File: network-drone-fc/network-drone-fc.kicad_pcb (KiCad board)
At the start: 4 copper layers, 27 x 27 mm, 4 parts

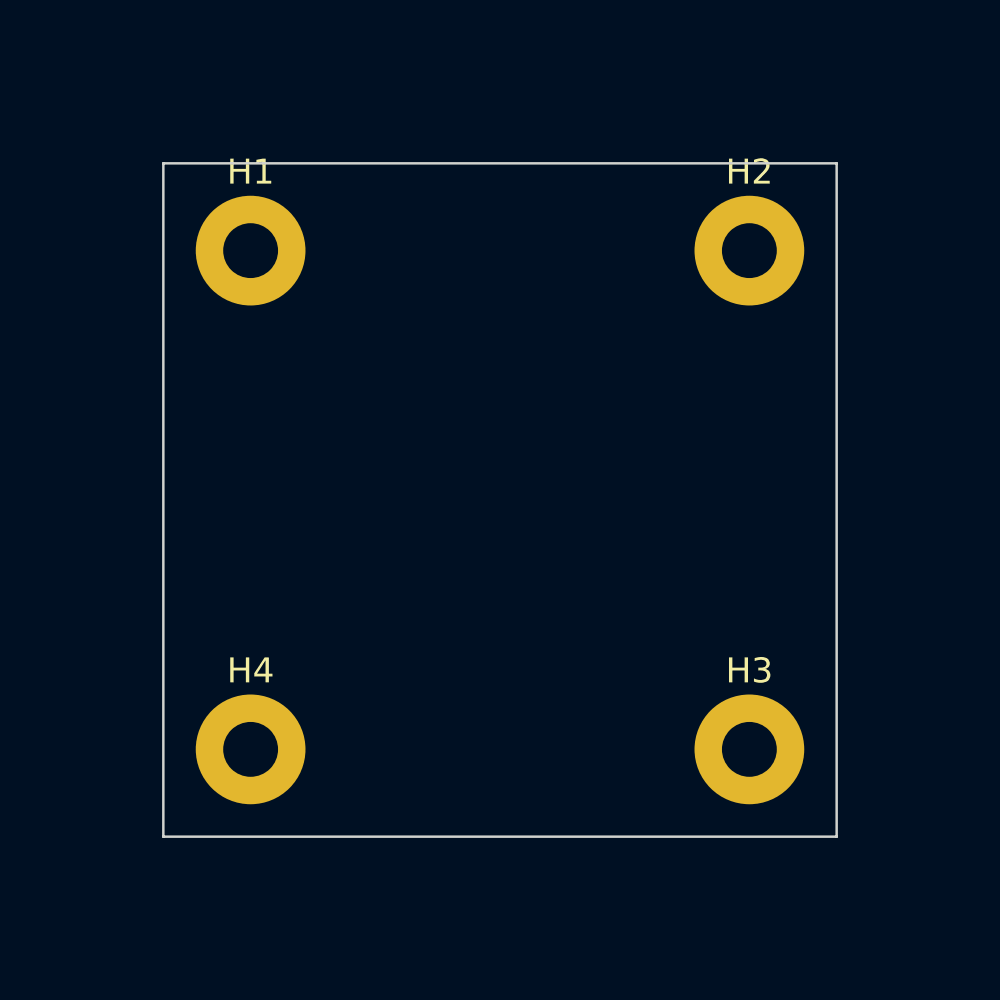
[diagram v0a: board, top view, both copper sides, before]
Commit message: Grow board to 36x36 mm so all parts fit on one side for hot-plate reflow
Keeps the 20x20 M2 holes to stack on the smaller ESC.
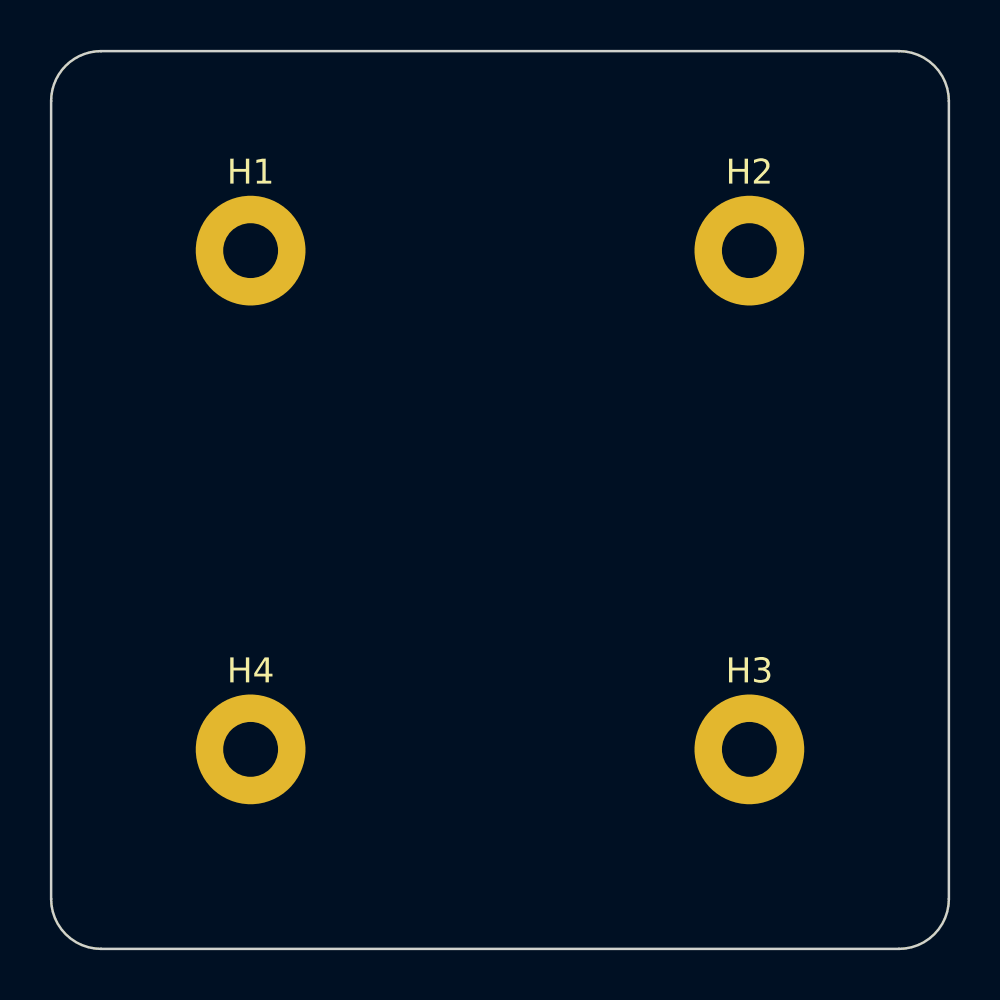
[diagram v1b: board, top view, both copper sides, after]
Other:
- board size 27 x 27 mm -> 36 x 36 mm
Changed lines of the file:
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@@
 		(embedded_fonts no)
 	)
-	(gr_line
-		(start 86.5 86.5)
-		(end 113.5 86.5)
+	(gr_arc
+		(start 116 82)
+		(mid 117.414213 82.585786)
+		(end 118 84)
 		(stroke
 			(width 0.1)
@@
 	)
 	(gr_line
-		(start 113.5 113.5)
-		(end 86.5 113.5)
+		(start 118 84)
+		(end 118 116)
+		(stroke
+			(width 0.1)
+			(type default)
+		)
+		(layer "Edge.Cuts")
+	)
+	(gr_arc
+		(start 82 84)
+		(mid 82.585786 82.585786)
+		(end 84 82)
 		(stroke
 			(width 0.1)
@@
 	)
 	(gr_line
-		(start 113.5 86.5)
-		(end 113.5 113.5)
+		(start 116 118)
+		(end 84 118)
+		(stroke
+			(width 0.1)
+			(type default)
+		)
+		(layer "Edge.Cuts")
+	)
+	(gr_arc
+		(start 84 118)
+		(mid 82.585786 117.414213)
+		(end 82 116)
 		(stroke
 			(width 0.1)
@@
 	)
 	(gr_line
-		(start 86.5 113.5)
-		(end 86.5 86.5)
+		(start 84 82)
+		(end 116 82)
 		(stroke
 			(width 0.1)
+			(type default)
+		)
+		(layer "Edge.Cuts")
+	)
+	(gr_line
+		(start 82 116)
+		(end 82 84)
+		(stroke
+			(width 0.1)
+			(type default)
+		)
+		(layer "Edge.Cuts")
+	)
+	(gr_arc
+		(start 118 116)
+		(mid 117.414213 117.414213)
+		(end 116 118)
+		(stroke
+			(width 0.1)
